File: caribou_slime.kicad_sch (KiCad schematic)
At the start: 36 parts, among them J1 BATT JST, Q1 AO3145, U1 ESP32-C3_SUPERMINI, U2 BMI270, U3 FS312F-G, U4 FS8205A, U5 TP4056, U6 ME6211C33M5G

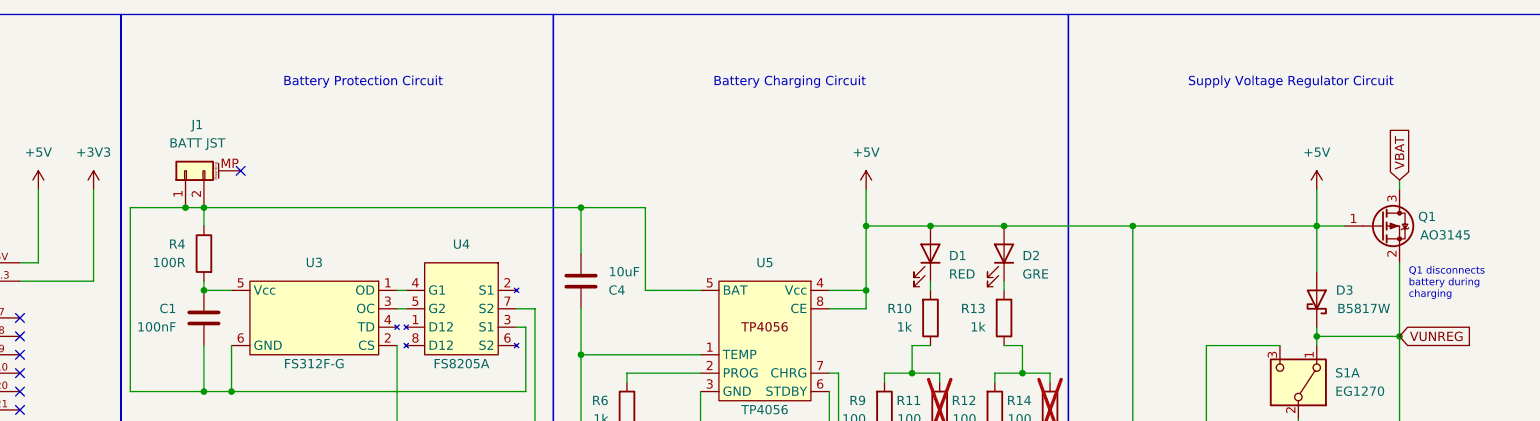
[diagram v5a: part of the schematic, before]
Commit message: fix(schematic): Fix shorted battery nets
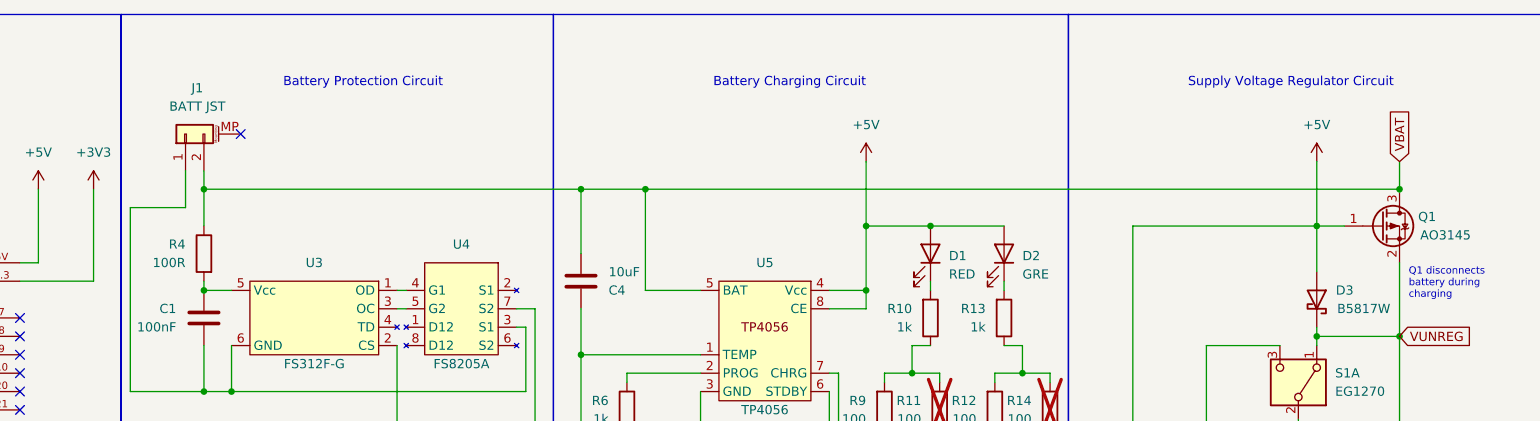
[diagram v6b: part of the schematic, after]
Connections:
- net VBAT: now also C4.2, J1.2 (Pin_2), R4.1, U5.5 (BAT)
- net at C1.2, J1.1 (Pin_1), U3.6 (GND)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: no longer C4.2, J1.2 (Pin_2), R4.1, U5.5 (BAT)
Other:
- moved on the sheet: J1
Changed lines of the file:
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@@
 (kicad_sch (version 20230121) (generator eeschema)
   (paper "A4")
+  (junction (at 148.59 36.83) (diameter 0) (color 0 0 0 0)
+  )
   (junction (at 194.31 62.23) (diameter 0) (color 0 0 0 0)
   )
   (junction (at 100.33 64.77) (diameter 0) (color 0 0 0 0)
   )
-  (junction (at 148.59 39.37) (diameter 0) (color 0 0 0 0)
-  )
   (junction (at 148.59 93.98) (diameter 0) (color 0 0 0 0)
   )
@@
   (junction (at 165.1 93.98) (diameter 0) (color 0 0 0 0)
   )
+  (junction (at 96.52 36.83) (diameter 0) (color 0 0 0 0)
+  )
   (junction (at 148.59 59.69) (diameter 0) (color 0 0 0 0)
   )
+  (junction (at 157.48 36.83) (diameter 0) (color 0 0 0 0)
+  )
   (junction (at 72.39 146.05) (diameter 0) (color 0 0 0 0)
   )
@@
   (junction (at 154.94 72.39) (diameter 0) (color 0 0 0 0)
   )
-  (junction (at 93.98 39.37) (diameter 0) (color 0 0 0 0)
-  )
   (junction (at 224.79 93.98) (diameter 0) (color 0 0 0 0)
   )
@@
   (junction (at 120.65 143.51) (diameter 0) (color 0 0 0 0)
   )
-  (junction (at 207.01 41.91) (diameter 0) (color 0 0 0 0)
-  )
   (junction (at 242.57 93.98) (diameter 0) (color 0 0 0 0)
   )
-  (junction (at 224.79 41.91) (diameter 0) (color 0 0 0 0)
-  )
   (junction (at 187.96 50.8) (diameter 0) (color 0 0 0 0)
   )
@@
   (junction (at 59.69 158.75) (diameter 0) (color 0 0 0 0)
   )
+  (junction (at 261.62 36.83) (diameter 0) (color 0 0 0 0)
+  )
   (junction (at 154.94 83.82) (diameter 0) (color 0 0 0 0)
   )
   (junction (at 250.19 41.91) (diameter 0) (color 0 0 0 0)
-  )
-  (junction (at 96.52 39.37) (diameter 0) (color 0 0 0 0)
   )
   (junction (at 154.94 93.98) (diameter 0) (color 0 0 0 0)
@@
   (no_connect (at 35.56 69.85))
   (no_connect (at 107.95 168.91))
-  (no_connect (at 101.6 34.29))
+  (no_connect (at 101.6 29.21))
   (wire (pts (xy 245.11 58.42) (xy 234.95 58.42))
     (stroke (width 0) (type default))
@@
     (stroke (width 0) (type default))
   )
+  (wire (pts (xy 148.59 36.83) (xy 148.59 45.72))
+    (stroke (width 0) (type default))
+  )
   (wire (pts (xy 165.1 62.23) (xy 154.94 62.23))
     (stroke (width 0) (type default))
@@
     (stroke (width 0) (type default))
   )
-  (wire (pts (xy 96.52 39.37) (xy 148.59 39.37))
+  (wire (pts (xy 96.52 36.83) (xy 148.59 36.83))
     (stroke (width 0) (type default))
   )
@@
     (stroke (width 0) (type default))
   )
-  (wire (pts (xy 96.52 39.37) (xy 96.52 41.91))
+  (wire (pts (xy 157.48 36.83) (xy 261.62 36.83))
     (stroke (width 0) (type default))
   )
@@
     (stroke (width 0) (type default))
   )
+  (wire (pts (xy 96.52 34.29) (xy 96.52 36.83))
+    (stroke (width 0) (type default))
+  )
   (wire (pts (xy 224.79 93.98) (xy 224.79 96.52))
     (stroke (width 0) (type default))
@@
     (stroke (width 0) (type default))
   )
-  (wire (pts (xy 148.59 39.37) (xy 157.48 39.37))
+  (wire (pts (xy 148.59 36.83) (xy 157.48 36.83))
     (stroke (width 0) (type default))
   )
@@
     (stroke (width 0) (type default))
   )
-  (wire (pts (xy 187.96 36.83) (xy 187.96 41.91))
+  (wire (pts (xy 187.96 33.02) (xy 187.96 41.91))
     (stroke (width 0) (type default))
   )
@@
     (stroke (width 0) (type default))
   )
+  (wire (pts (xy 96.52 36.83) (xy 96.52 41.91))
+    (stroke (width 0) (type default))
+  )
   (wire (pts (xy 142.24 53.34) (xy 142.24 93.98))
     (stroke (width 0) (type default))
@@
     (stroke (width 0) (type default))
   )
-  (wire (pts (xy 207.01 41.91) (xy 224.79 41.91))
-    (stroke (width 0) (type default))
-  )
   (wire (pts (xy 113.03 146.05) (xy 113.03 147.32))
     (stroke (width 0) (type default))
@@
     (stroke (width 0) (type default))
   )
-  (wire (pts (xy 96.52 39.37) (xy 93.98 39.37))
-    (stroke (width 0) (type default))
-  )
   (wire (pts (xy 261.62 69.85) (xy 261.62 57.15))
     (stroke (width 0) (type default))
@@
     (stroke (width 0) (type default))
   )
-  (wire (pts (xy 148.59 39.37) (xy 148.59 45.72))
-    (stroke (width 0) (type default))
-  )
   (wire (pts (xy 154.94 83.82) (xy 154.94 93.98))
     (stroke (width 0) (type default))
@@
     (stroke (width 0) (type default))
   )
+  (wire (pts (xy 93.98 34.29) (xy 93.98 39.37))
+    (stroke (width 0) (type default))
+  )
   (wire (pts (xy 71.12 163.83) (xy 77.47 163.83))
     (stroke (width 0) (type default))
   )
-  (wire (pts (xy 250.19 36.83) (xy 250.19 41.91))
+  (wire (pts (xy 250.19 33.02) (xy 250.19 41.91))
     (stroke (width 0) (type default))
   )
@@
     (stroke (width 0) (type default))
   )
-  (wire (pts (xy 86.36 39.37) (xy 93.98 39.37))
-    (stroke (width 0) (type default))
-  )
-  (wire (pts (xy 157.48 39.37) (xy 157.48 50.8))
+  (wire (pts (xy 157.48 36.83) (xy 157.48 50.8))
     (stroke (width 0) (type default))
   )
@@
     (stroke (width 0) (type default))
   )
-  (wire (pts (xy 261.62 35.56) (xy 261.62 36.83))
+  (wire (pts (xy 261.62 33.02) (xy 261.62 36.83))
     (stroke (width 0) (type default))
   )
   (wire (pts (xy 81.28 49.53) (xy 81.28 36.83))
+    (stroke (width 0) (type default))
+  )
+  (wire (pts (xy 93.98 39.37) (xy 86.36 39.37))
     (stroke (width 0) (type default))
   )
@@
     )
   )
-  (global_label "VBAT" (shape input) (at 261.62 35.56 90) (fields_autoplaced)
+  (global_label "VBAT" (shape input) (at 261.62 33.02 90) (fields_autoplaced)
     (effects (font (size 1.27 1.27)) (justify left))
-    (property "Intersheetrefs" "${INTERSHEET_REFS}" (at 261.62 28.16 90)
+    (property "Intersheetrefs" "${INTERSHEET_REFS}" (at 261.62 25.62 90)
       (effects (font (size 1.27 1.27)) (justify left) hide)
     )
@@
     )
   )
-  (symbol (lib_id "Connector_Generic_MountingPin:Conn_01x02_MountingPin") (at 93.98 34.29 90) (unit 1)
+  (symbol (lib_id "Connector_Generic_MountingPin:Conn_01x02_MountingPin") (at 93.98 29.21 90) (unit 1)
     (in_bom yes) (on_board yes) (dnp no)
-    (property "Reference" "J1" (at 95.6056 27.94 90)
+    (property "Reference" "J1" (at 95.6056 22.86 90)
       (effects (font (size 1.27 1.27)))
     )
-    (property "Value" "BATT JST" (at 95.6056 30.48 90)
+    (property "Value" "BATT JST" (at 95.6056 25.4 90)
       (effects (font (size 1.27 1.27)))
     )
-    (property "Footprint" "Connector_JST:JST_PH_B2B-PH-K_1x02_P2.00mm_Vertical" (at 93.98 34.29 0)
-      (effects (font (size 1.27 1.27)) hide)
-    )
-    (property "Datasheet" "~" (at 93.98 34.29 0)
+    (property "Footprint" "Connector_JST:JST_PH_B2B-PH-K_1x02_P2.00mm_Vertical" (at 93.98 29.21 0)
+      (effects (font (size 1.27 1.27)) hide)
+    )
+    (property "Datasheet" "~" (at 93.98 29.21 0)
       (effects (font (size 1.27 1.27)) hide)
     )
@@
     )
   )
-  (symbol (lib_id "power:+5V") (at 250.19 36.83 0) (mirror y) (unit 1)
+  (symbol (lib_id "power:+5V") (at 250.19 33.02 0) (mirror y) (unit 1)
     (in_bom yes) (on_board yes) (dnp no)
-    (property "Reference" "#PWR010" (at 250.19 40.64 0)
-      (effects (font (size 1.27 1.27)) hide)
-    )
-    (property "Value" "+5V" (at 250.19 31.75 0)
+    (property "Reference" "#PWR010" (at 250.19 36.83 0)
+      (effects (font (size 1.27 1.27)) hide)
+    )
+    (property "Value" "+5V" (at 250.19 27.94 0)
       (effects (font (size 1.27 1.27)))
     )
-    (property "Footprint" "" (at 250.19 36.83 0)
-      (effects (font (size 1.27 1.27)) hide)
-    )
-    (property "Datasheet" "" (at 250.19 36.83 0)
+    (property "Footprint" "" (at 250.19 33.02 0)
+      (effects (font (size 1.27 1.27)) hide)
+    )
+    (property "Datasheet" "" (at 250.19 33.02 0)
       (effects (font (size 1.27 1.27)) hide)
     )
@@
     )
   )
-  (symbol (lib_id "power:+5V") (at 187.96 36.83 0) (mirror y) (unit 1)
+  (symbol (lib_id "power:+5V") (at 187.96 33.02 0) (mirror y) (unit 1)
     (in_bom yes) (on_board yes) (dnp no)
-    (property "Reference" "#PWR09" (at 187.96 40.64 0)
-      (effects (font (size 1.27 1.27)) hide)
-    )
-    (property "Value" "+5V" (at 187.96 31.75 0)
+    (property "Reference" "#PWR09" (at 187.96 36.83 0)
+      (effects (font (size 1.27 1.27)) hide)
+    )
+    (property "Value" "+5V" (at 187.96 27.94 0)
       (effects (font (size 1.27 1.27)))
     )
-    (property "Footprint" "" (at 187.96 36.83 0)
-      (effects (font (size 1.27 1.27)) hide)
-    )
-    (property "Datasheet" "" (at 187.96 36.83 0)
-      (effects (font (size 1.27 1.27)) hide)
-    )
+    (property "Footprint" "" (at 187.96 33.02 0)
+      (effects (font (size 1.27 1.27)) hide)
+    )
+    (property "Datasheet" "" (at 187.96 33.02 0)
+      (effects (font (size 1.27 1.27)) hide)
+    )

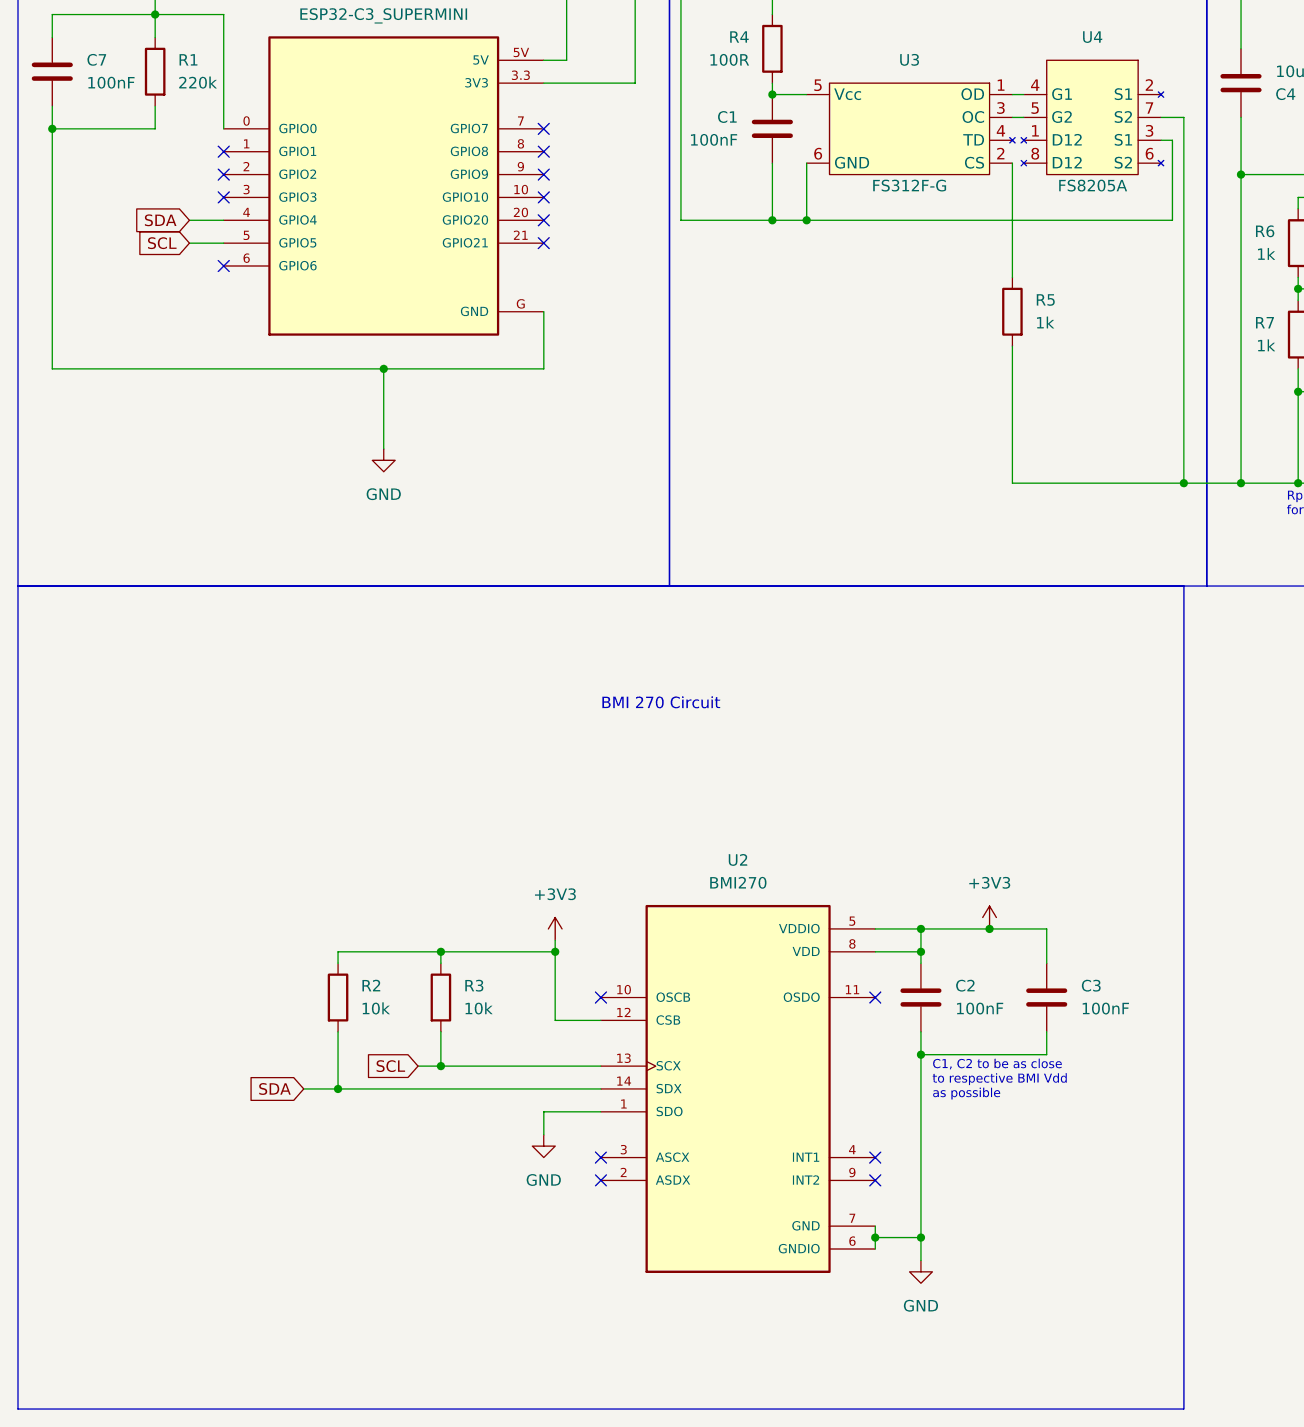
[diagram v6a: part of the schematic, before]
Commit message: feat(schematic): Add BNO085 as alternate IMU
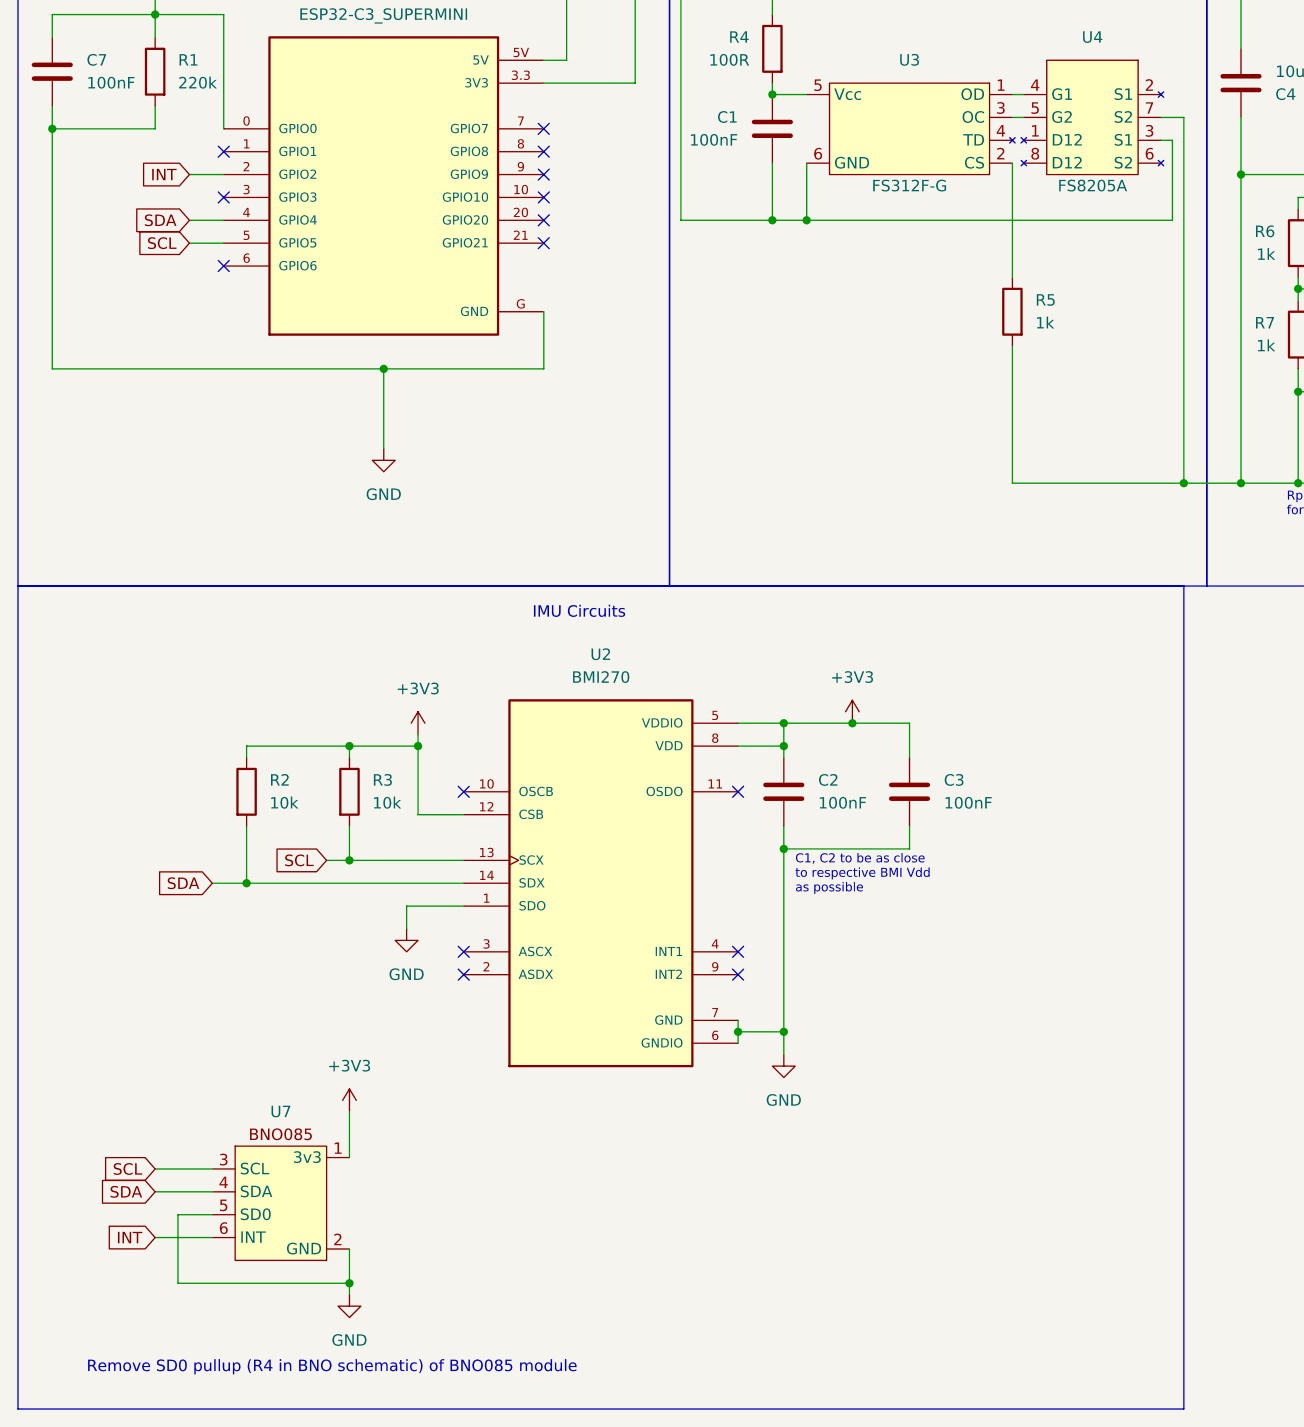
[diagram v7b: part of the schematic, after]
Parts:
- added U7: ~, symbol BNO:BNO085
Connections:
- net +3V3: now also U7.1 (3v3)
- net GND: now also U7.2 (GND), U7.5 (SD0)
- net SCL: now also U7.3 (SCL)
- net SDA: now also U7.4 (SDA)
- net INT: now reaches U1.2 (GPIO2)
- net INT: now also U7.6 (INT)
- no-connect marks 18 -> 17
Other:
- note added: "IMU Circuits"
- note added: "Remove SD0 pullup (R4 in BNO schematic) of BNO085 module"
- note removed: "BMI 270 Circuit"
- moved on the sheet: C2, C3, R2, R3, U2

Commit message: feat(pcb): Add BNO085 module
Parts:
- U7: footprint (none) -> BNO:BNO085_Module
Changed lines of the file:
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@@
       (effects (font (size 1.27 1.27)))
     )
-    (property "Footprint" "" (at 41.91 181.61 0)
+    (property "Footprint" "BNO:BNO085_Module" (at 41.91 181.61 0)
       (effects (font (size 1.27 1.27)) hide)
     )
